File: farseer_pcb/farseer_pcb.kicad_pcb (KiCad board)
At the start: 4 copper layers, 32 x 18 mm, 38 parts, among them J1 USB_C_10137062-00021LF, J2 UMC_JACK_SMD, J3 UMC_JACK_SMD, U1 MAX865EUA+, U2 UAF42_SMA, U3 UAF42_SMA, U4 OPA381

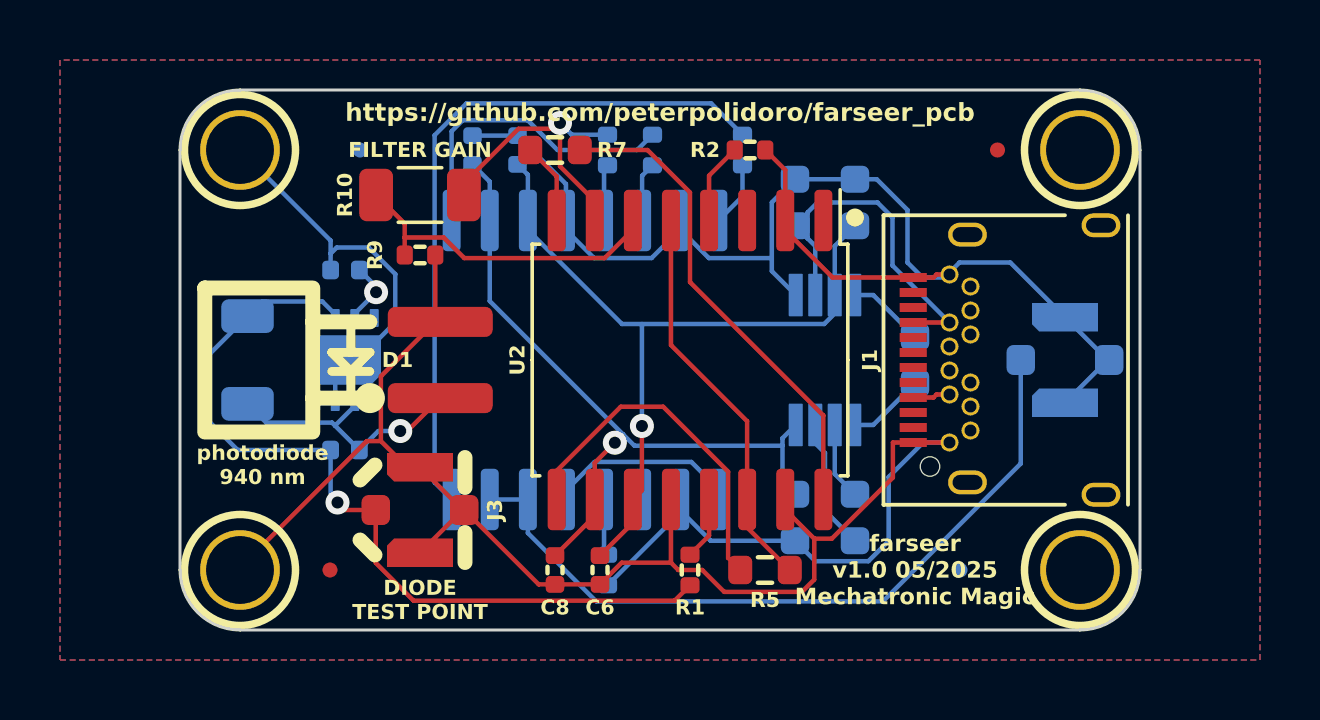
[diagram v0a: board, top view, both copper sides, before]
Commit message: Begin board resize
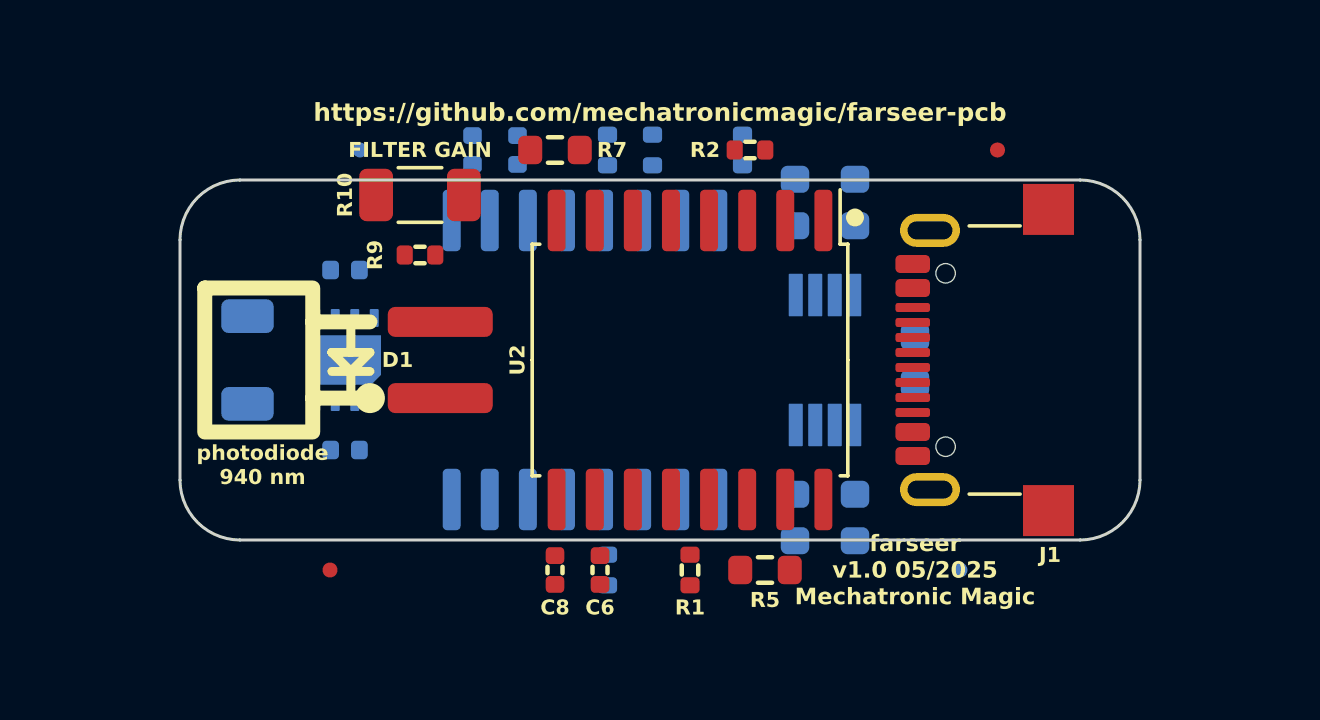
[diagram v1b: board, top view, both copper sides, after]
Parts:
- removed H1, H2, H3, H4: MOUNTING_HOLE_2, Janelia:MOUNTING_HOLE_2
- removed J2, J3: UMC_JACK_SMD, Janelia:UMC_AMPHENOL_A-1JB
- J1: value USB_C_10137062-00021LF -> Connector_USB_C_Receptacle_USB2.0_16P_GT-USB-7047C; footprint Janelia:USB_C_Receptacle_Amphenol_10137062-00021LF -> Janelia:USB_C_Receptacle_GT-USB-7047C_16P_TopMnt_Horizontal
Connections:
- net /filter/BANDPASS_BUFFERED renamed /BANDPASS_BUFFERED
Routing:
- net /GND: track 151.5 -> 0.00 mm
- net /V5+: track 37.9 -> 0.00 mm, vias 1 -> 0
- net /PHOTODIODE_SIG: track 28.1 -> 0.00 mm, vias 1 -> 0
- net /V10+: track 25.5 -> 0.00 mm, vias 1 -> 0
- net /BANDPASS_BUFFERED: track 25.1 -> 0.00 mm
- net /V10-: track 24.2 -> 0.00 mm, vias 1 -> 0
- net Net-(U3-BPVo): track 23.5 -> 0.00 mm
- net Net-(U2-Fadj2): track 16.3 -> 0.00 mm
- net /filter/HIGHPASS: track 13.3 -> 0.00 mm
- net Net-(U2-Fadj1): track 11.9 -> 0.00 mm
- net Net-(U2-AAin-): track 11.0 -> 0.00 mm
- net Net-(U3-Fadj1): track 10.4 -> 0.00 mm
- net /filter/HIGHPASS_AMPLIFIED: track 9.82 -> 0.00 mm, vias 1 -> 0
- net Net-(D1-K): track 8.84 -> 0.00 mm, vias 1 -> 0
- net /filter/LOWPASS: track 6.50 -> 0.00 mm
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- removed copper zone on B.Cu, net /GND
- removed copper zone on F.Cu, net /GND
- removed copper zone on In1.Cu, net /GND
- removed copper zone on In2.Cu, net /V5+
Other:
- board size 32 x 18 mm -> 32 x 12 mm
- board text added: "https://github.com/mechatronicmagic/farseer-pcb"
- board text removed: "DIODE TEST POINT"
- board text removed: "FILTERED OUTPUT"
- board text removed: "https://github.com/peterpolidoro/farseer_pcb"
